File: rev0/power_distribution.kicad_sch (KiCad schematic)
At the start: 86 parts, among them Q1 PMOS, Q10 2PNP, Q11 2NPN, Q12 PMOS, Q13 2PNP, Q14 2PNP, Q15 2PNP, Q2 PMOS, Q3 2NPN, Q4 PMOS, Q5 PMOS, Q6 PMOS, Q7 PMOS, Q8 2NPN, Q9 PMOS, U1 PAC1954

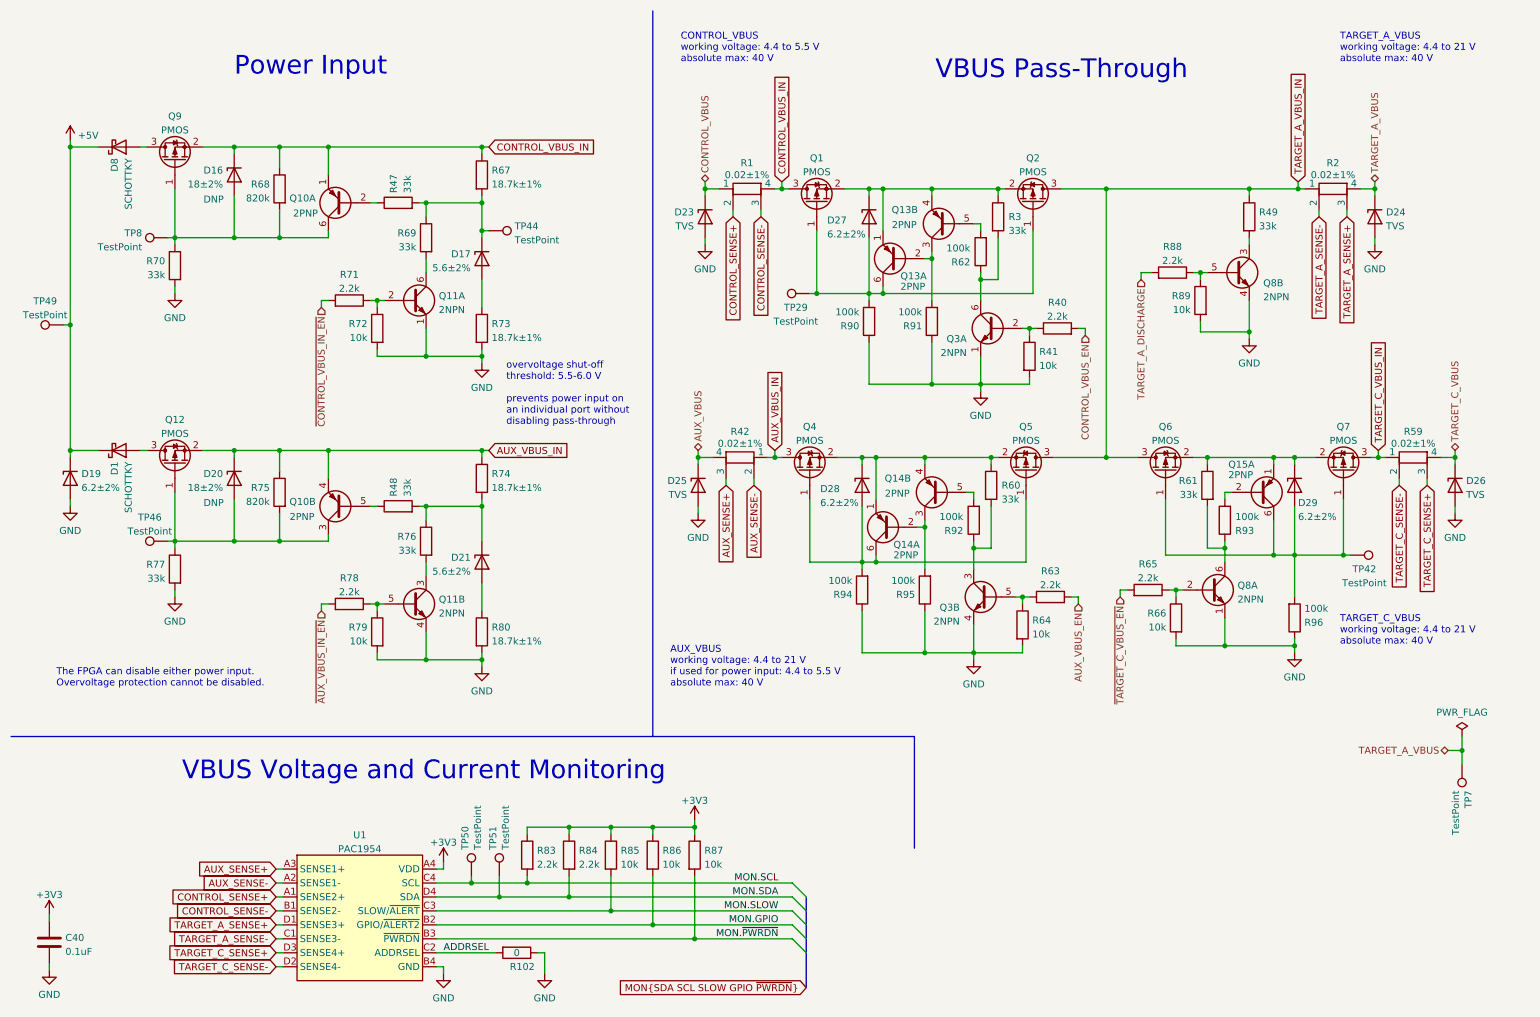
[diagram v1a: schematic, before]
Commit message: hardware: update component selections
- fix overheating of TVS diodes D23-D26 starting at 27 V
- change absolute maximum VBUS from 40 V to 30 V
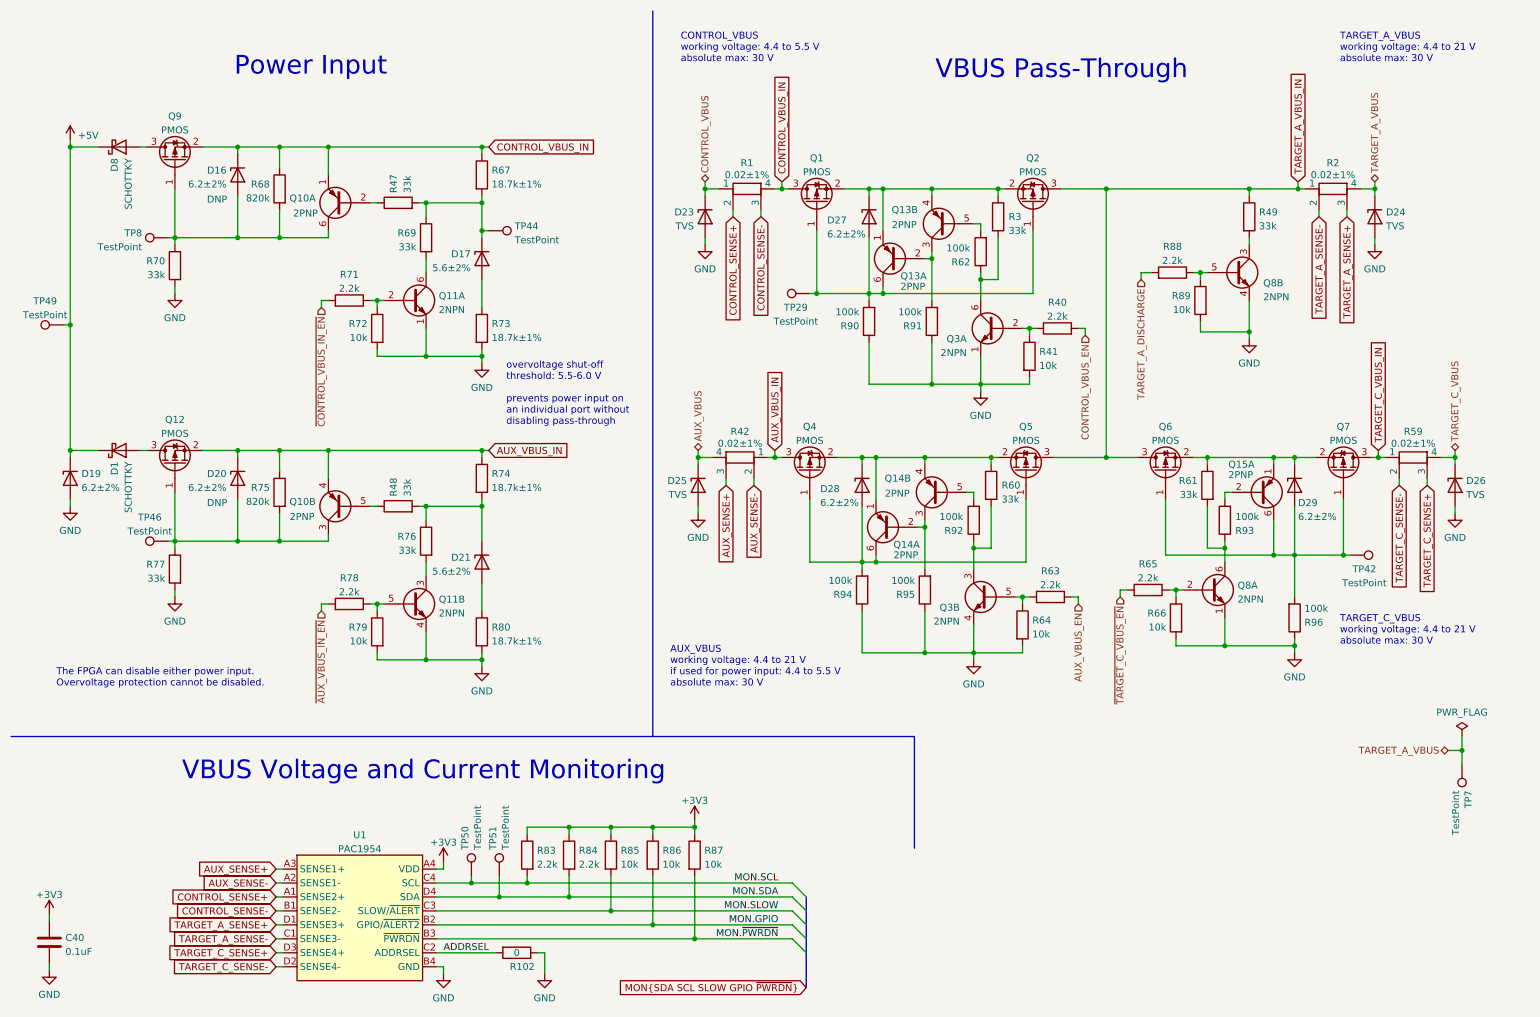
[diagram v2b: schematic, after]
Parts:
- D16, D20: value 18±2% -> 6.2±2%; Part Number BZX884-B18,315 -> BZX884-B6V2,315
- D23, D24, D25, D26: Part Number PESD24VS1UL,315 -> PESD36VS1UL,315
- Q12, Q9: Manufacturer Panjit -> Yangzhou Yangjie; Part Number PJA3441_R1_00001 -> YJL3401A; Substitution (none) -> Alpha & Omega AO3401A
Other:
- note added: "AUX_VBUS working voltage: 4.4 to 21 V if used for power input: 4.4 to 5.5 V absolute max: 30 V"
- note added: "CONTROL_VBUS working voltage: 4.4 to 5.5 V absolute max: 30 V"
- note added: "TARGET_A_VBUS working voltage: 4.4 to 21 V absolute max: 30 V"
- note added: "TARGET_C_VBUS working voltage: 4.4 to 21 V absolute max: 30 V"
- note removed: "AUX_VBUS working voltage: 4.4 to 21 V if used for power input: 4.4 to 5.5 V absolute max: 40 V"
- note removed: "CONTROL_VBUS working voltage: 4.4 to 5.5 V absolute max: 40 V"
- note removed: "TARGET_A_VBUS working voltage: 4.4 to 21 V absolute max: 40 V"
- note removed: "TARGET_C_VBUS working voltage: 4.4 to 21 V absolute max: 40 V"
- moved on the sheet: D16, D20

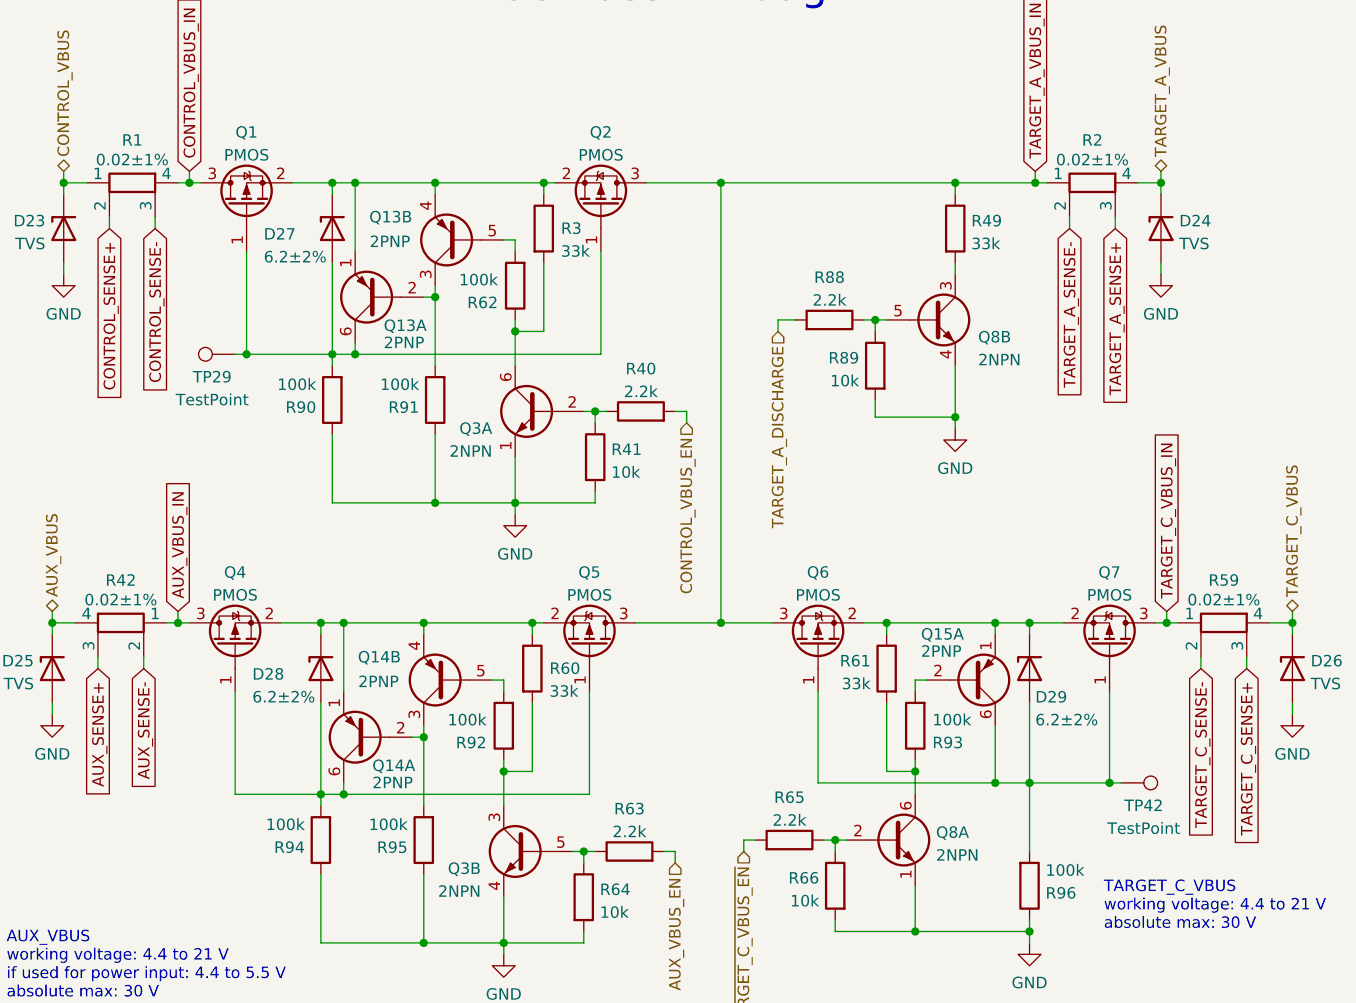
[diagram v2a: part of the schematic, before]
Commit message: hardware: update VBUS passthrough FETs
- reduce on resistance
- improve power dissipation
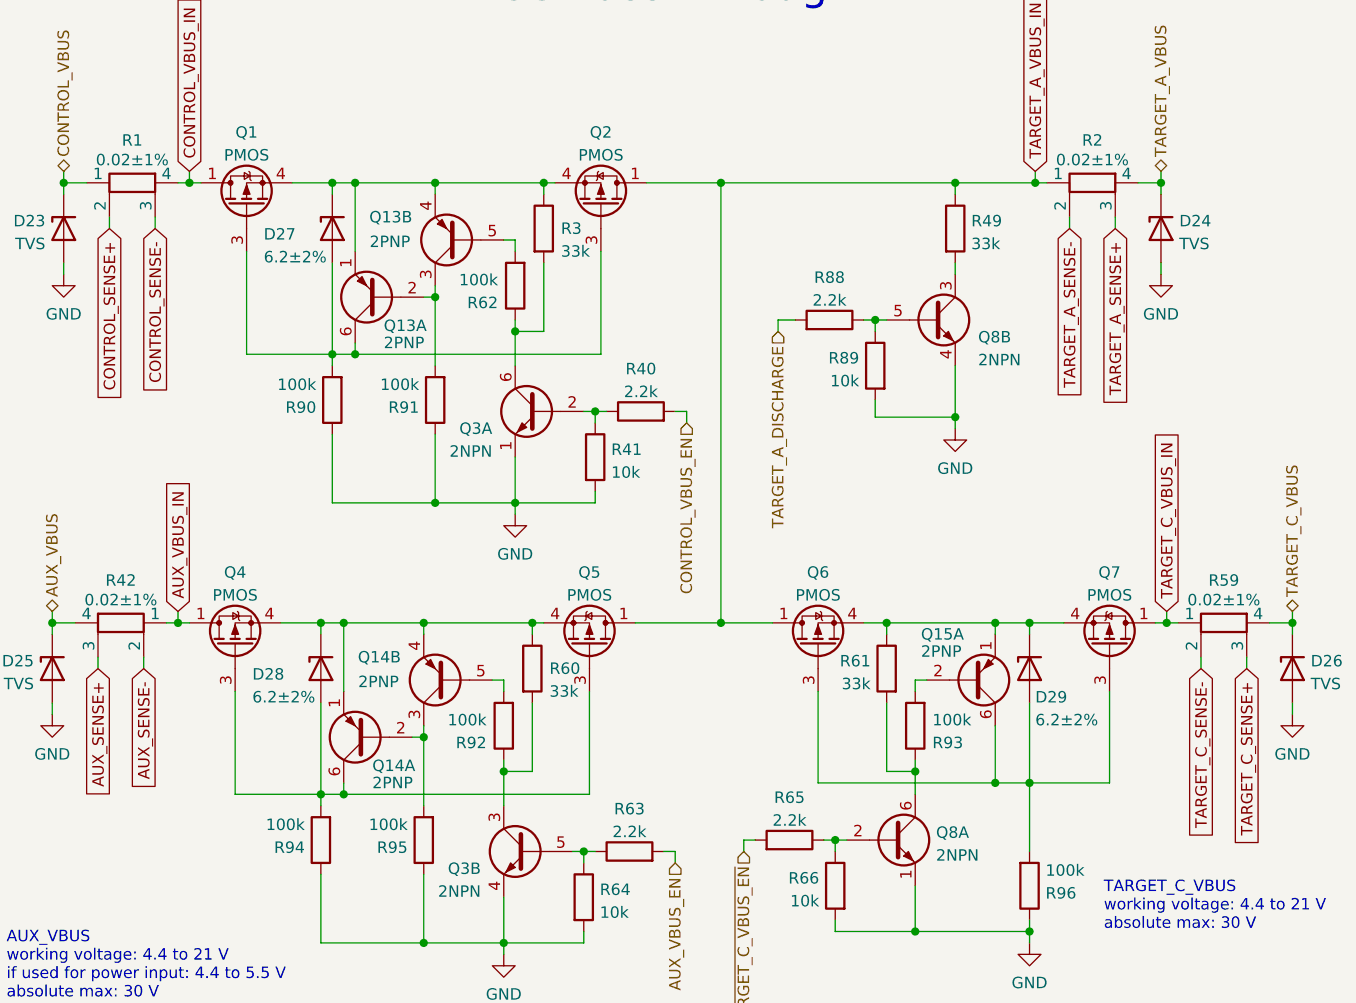
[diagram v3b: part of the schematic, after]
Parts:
- removed TP29, TP42: TestPoint, TestPoint:TestPoint_Pad_D1.0mm, symbol Connector:TestPoint
- Q1, Q2, Q4, Q5, Q6, Q7: footprint Package_TO_SOT_SMD:SOT-23-3 -> luna:Vishay_PowerPAK_SC70-6L_Single; symbol Device:Q_PMOS_GSD -> Transistor_FET:SiA449DJ; Manufacturer Panjit -> Diodes Inc.; Part Number PJA3441_R1_00001 -> DMP3028LFDE-7; Substitution (none) -> DMP3028LFDE-13, Nexperia PMPB27EP,115, PMPB16EPX, Vishay SI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
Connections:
- net AUX_VBUS_IN: now also Q4.1 (D); no longer Q4.3 (D)
- net CONTROL_VBUS_IN: now also Q1.1 (D); no longer Q1.3 (D)
- net TARGET_A_VBUS_IN: now also Q2.1 (D), Q5.1 (D), Q6.1 (D); no longer Q2.3 (D), Q5.3 (D), Q6.3 (D)
- net TARGET_C_VBUS_IN: now also Q7.1 (D); no longer Q7.3 (D)
- net at D27.1 (K), Q13.1 (E1), Q13.4 (E2)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: now also Q1.4 (S), Q2.4 (S); no longer Q1.2 (S), Q2.2 (S)
- net at D27.2 (A), Q13.6 (C1), R90.2: now also Q1.3 (G), Q2.3 (G); no longer Q1.1 (G), Q2.1 (G)
- net at D29.2 (A), Q15.6 (C1), R96.2: now also Q6.3 (G), Q7.3 (G); no longer Q6.1 (G), Q7.1 (G)
- net at D29.1 (K), Q15.1 (E1), R61.1: now also Q6.4 (S), Q7.4 (S); no longer Q6.2 (S), Q7.2 (S)
- net at D28.1 (K), Q14.1 (E1), Q14.4 (E2)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: now also Q4.4 (S), Q5.4 (S); no longer Q4.2 (S), Q5.2 (S)
- net at D28.2 (A), Q14.6 (C1), R94.2: now also Q4.3 (G), Q5.3 (G); no longer Q4.1 (G), Q5.1 (G)
